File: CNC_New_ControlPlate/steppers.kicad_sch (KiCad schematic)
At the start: 6 parts

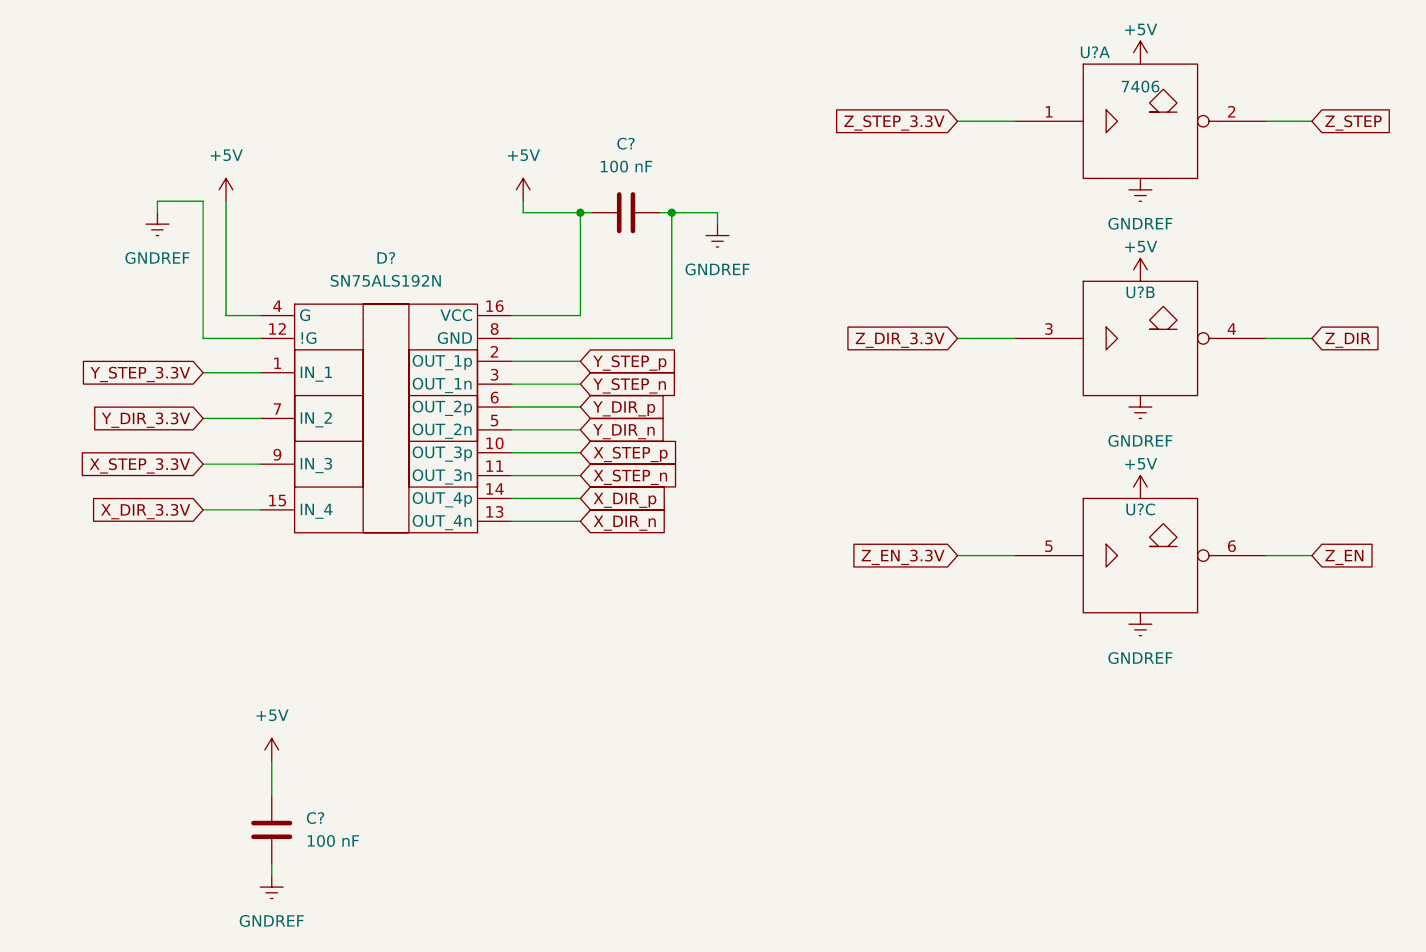
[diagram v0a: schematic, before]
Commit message: [*] Исправлены ошибки с выходами питания. [+] Добавлены обозначения элементов
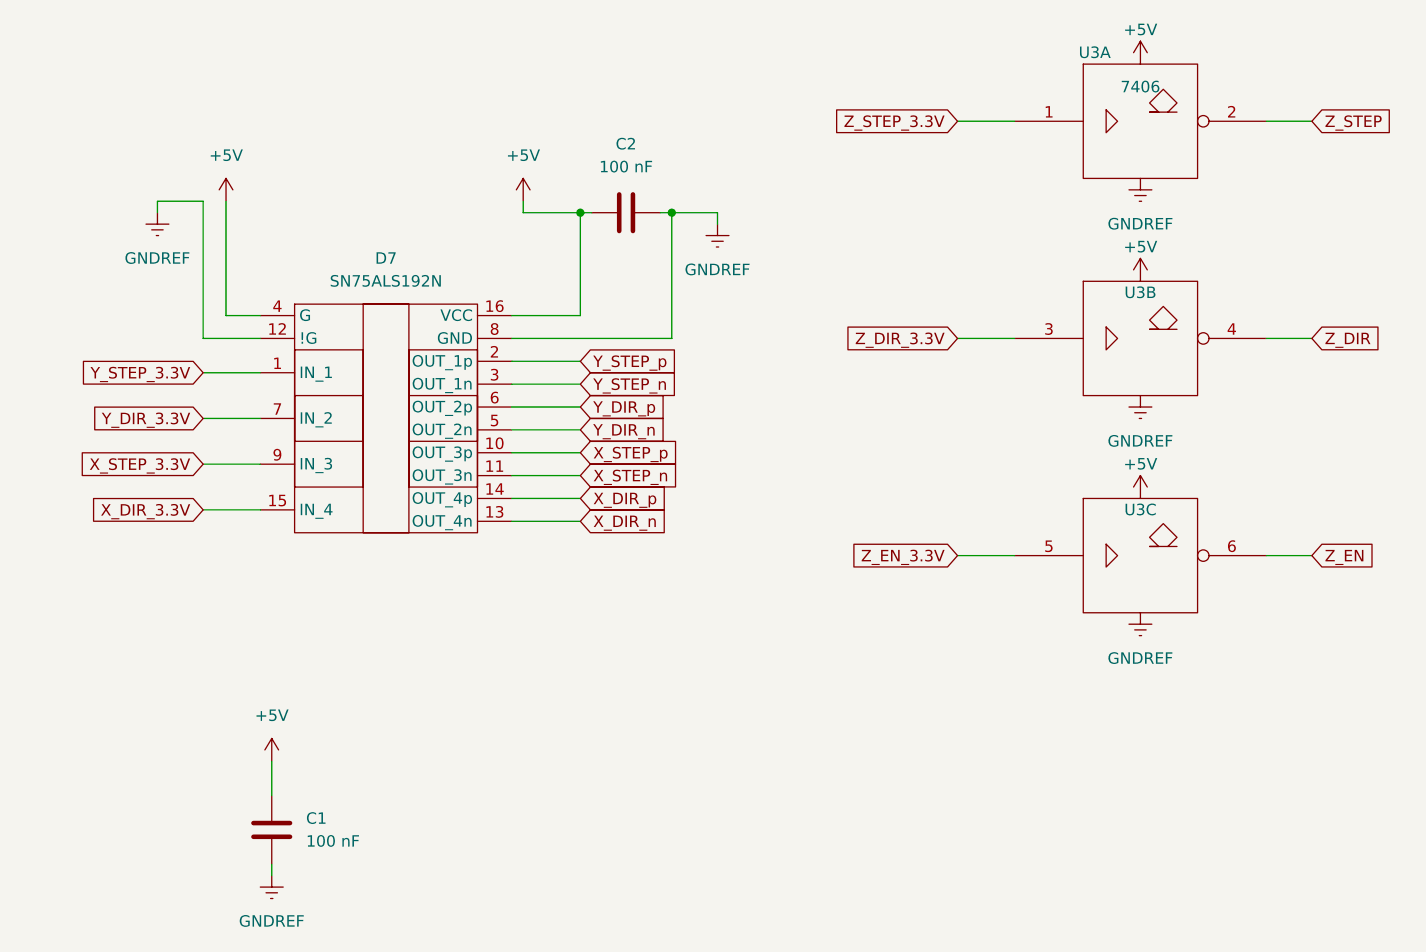
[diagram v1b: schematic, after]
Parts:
- gave numbers to parts that had none: 4
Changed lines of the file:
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@@
   (symbol (lib_id "power:+5V") (at 45.72 40.64 0) (unit 1)
     (in_bom yes) (on_board yes) (fields_autoplaced)
-    (property "Reference" "#PWR?" (id 0) (at 45.72 44.45 0)
+    (property "Reference" "#PWR027" (id 0) (at 45.72 44.45 0)
       (effects (font (size 1.27 1.27)) hide)
     )
@@
   (symbol (lib_id "power:+5V") (at 147.32 49.53 0) (unit 1)
     (in_bom yes) (on_board yes)
-    (property "Reference" "#PWR?" (id 0) (at 147.32 53.34 0)
+    (property "Reference" "#PWR034" (id 0) (at 147.32 53.34 0)
       (effects (font (size 1.27 1.27)) hide)
     )
@@
   (symbol (lib_id "74xx_IEEE:7406") (at 147.32 55.88 0) (unit 2)
     (in_bom yes) (on_board yes)
-    (property "Reference" "U?" (id 0) (at 147.32 50.8 0))
+    (property "Reference" "U3" (id 0) (at 147.32 50.8 0))
     (property "Value" "7406" (id 1) (at 147.32 46.99 0)
       (effects (font (size 1.27 1.27)) hide)
@@
   (symbol (lib_id "power:GNDREF") (at 147.32 62.23 0) (unit 1)
     (in_bom yes) (on_board yes) (fields_autoplaced)
-    (property "Reference" "#PWR?" (id 0) (at 147.32 68.58 0)
+    (property "Reference" "#PWR035" (id 0) (at 147.32 68.58 0)
       (effects (font (size 1.27 1.27)) hide)
     )
@@
   (symbol (lib_id "power:GNDREF") (at 38.1 41.91 0) (unit 1)
     (in_bom yes) (on_board yes) (fields_autoplaced)
-    (property "Reference" "#PWR?" (id 0) (at 38.1 48.26 0)
+    (property "Reference" "#PWR026" (id 0) (at 38.1 48.26 0)
       (effects (font (size 1.27 1.27)) hide)
     )
@@
   (symbol (lib_id "74xx_IEEE:7406") (at 147.32 31.75 0) (unit 1)
     (in_bom yes) (on_board yes)
-    (property "Reference" "U?" (id 0) (at 142.24 24.13 0))
+    (property "Reference" "U3" (id 0) (at 142.24 24.13 0))
     (property "Value" "7406" (id 1) (at 147.32 27.94 0))
     (property "Footprint" "" (id 2) (at 147.32 31.75 0)
@@
   (symbol (lib_id "power:GNDREF") (at 147.32 38.1 0) (unit 1)
     (in_bom yes) (on_board yes) (fields_autoplaced)
-    (property "Reference" "#PWR?" (id 0) (at 147.32 44.45 0)
+    (property "Reference" "#PWR033" (id 0) (at 147.32 44.45 0)
       (effects (font (size 1.27 1.27)) hide)
     )
@@
   (symbol (lib_id "power:+5V") (at 78.74 40.64 0) (unit 1)
     (in_bom yes) (on_board yes) (fields_autoplaced)
-    (property "Reference" "#PWR?" (id 0) (at 78.74 44.45 0)
+    (property "Reference" "#PWR030" (id 0) (at 78.74 44.45 0)
       (effects (font (size 1.27 1.27)) hide)
     )
@@
   (symbol (lib_id "EP2006:SN75ALS192N") (at 63.5 49.53 0) (unit 1)
     (in_bom yes) (on_board yes) (fields_autoplaced)
-    (property "Reference" "D?" (id 0) (at 63.5 46.99 0))
+    (property "Reference" "D7" (id 0) (at 63.5 46.99 0))
     (property "Value" "SN75ALS192N" (id 1) (at 63.5 49.53 0))
     (property "Footprint" "Package_DIP:DIP-16_W7.62mm_Socket" (id 2) (at 63.5 49.53 0)
@@
   (symbol (lib_id "Device:C") (at 90.17 41.91 90) (unit 1)
     (in_bom yes) (on_board yes) (fields_autoplaced)
-    (property "Reference" "C?" (id 0) (at 90.17 34.29 90))
+    (property "Reference" "C2" (id 0) (at 90.17 34.29 90))
     (property "Value" "100 nF" (id 1) (at 90.17 36.83 90))
     (property "Footprint" "Capacitor_SMD:C_0603_1608Metric_Pad1.08x0.95mm_HandSolder" (id 2) (at 93.98 40.9448 0)
@@
   (symbol (lib_id "Device:C") (at 50.8 110.49 180) (unit 1)
     (in_bom yes) (on_board yes) (fields_autoplaced)
-    (property "Reference" "C?" (id 0) (at 54.61 109.2199 0)
+    (property "Reference" "C1" (id 0) (at 54.61 109.2199 0)
       (effects (font (size 1.27 1.27)) (justify right))
     )
@@
   (symbol (lib_id "power:+5V") (at 147.32 73.66 0) (unit 1)
     (in_bom yes) (on_board yes)
-    (property "Reference" "#PWR?" (id 0) (at 147.32 77.47 0)
+    (property "Reference" "#PWR036" (id 0) (at 147.32 77.47 0)
       (effects (font (size 1.27 1.27)) hide)
     )
@@
   (symbol (lib_id "power:GNDREF") (at 100.33 43.18 0) (unit 1)
     (in_bom yes) (on_board yes) (fields_autoplaced)
-    (property "Reference" "#PWR?" (id 0) (at 100.33 49.53 0)
+    (property "Reference" "#PWR031" (id 0) (at 100.33 49.53 0)
       (effects (font (size 1.27 1.27)) hide)
     )
@@
   (symbol (lib_id "power:+5V") (at 147.32 25.4 0) (unit 1)
     (in_bom yes) (on_board yes)
-    (property "Reference" "#PWR?" (id 0) (at 147.32 29.21 0)
+    (property "Reference" "#PWR032" (id 0) (at 147.32 29.21 0)
       (effects (font (size 1.27 1.27)) hide)
     )
@@
   (symbol (lib_id "power:GNDREF") (at 147.32 86.36 0) (unit 1)
     (in_bom yes) (on_board yes) (fields_autoplaced)
-    (property "Reference" "#PWR?" (id 0) (at 147.32 92.71 0)
+    (property "Reference" "#PWR037" (id 0) (at 147.32 92.71 0)
       (effects (font (size 1.27 1.27)) hide)
     )
@@
   (symbol (lib_id "power:GNDREF") (at 50.8 115.57 0) (unit 1)
     (in_bom yes) (on_board yes) (fields_autoplaced)
-    (property "Reference" "#PWR?" (id 0) (at 50.8 121.92 0)
+    (property "Reference" "#PWR029" (id 0) (at 50.8 121.92 0)
       (effects (font (size 1.27 1.27)) hide)
     )
@@
   (symbol (lib_id "74xx_IEEE:7406") (at 147.32 80.01 0) (unit 3)
     (in_bom yes) (on_board yes)
-    (property "Reference" "U?" (id 0) (at 147.32 74.93 0))
+    (property "Reference" "U3" (id 0) (at 147.32 74.93 0))
     (property "Value" "7406" (id 1) (at 147.32 71.12 0)
       (effects (font (size 1.27 1.27)) hide)
@@
   (symbol (lib_id "power:+5V") (at 50.8 102.87 0) (unit 1)
     (in_bom yes) (on_board yes)
-    (property "Reference" "#PWR?" (id 0) (at 50.8 106.68 0)
-      (effects (font (size 1.27 1.27)) hide)
-    )
+    (property "Reference" "#PWR028" (id 0) (at 50.8 106.68 0)
+      (effects (font (size 1.27 1.27)) hide)
+    )

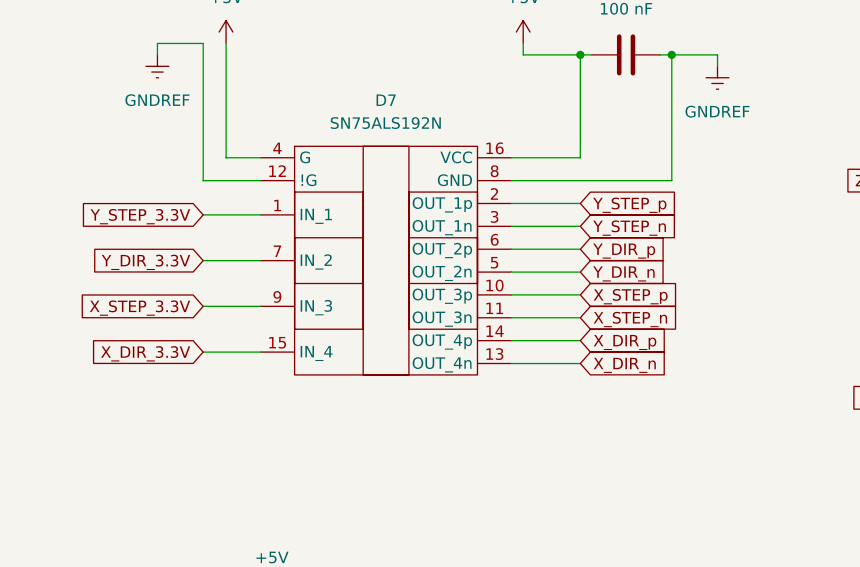
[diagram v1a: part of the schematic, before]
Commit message: [*] Порядок выводов на разъёме Others [*] Порядок выводов на разъёме Pause [*] Порядок подключения каналов на драйвере диф. линий [+] Начата расстановка pcb схемы
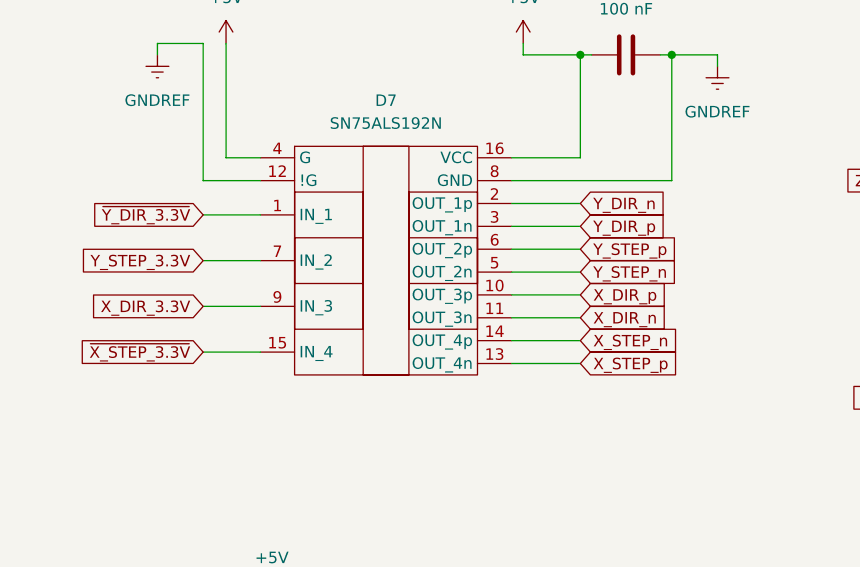
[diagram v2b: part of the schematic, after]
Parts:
- U3: footprint (none) -> Package_DIP:DIP-14_W7.62mm_Socket
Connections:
- net X_STEP_3.3V is gone; now on net X_DIR_3.3V: D7.9 (IN_3)
- net Y_DIR_3.3V is gone; now on net Y_STEP_3.3V: D7.7 (IN_2)
- net X_DIR_3.3V: no longer D7.15 (IN_4)
- net X_DIR_n: now also D7.11 (OUT_3n); no longer D7.13 (OUT_4n)
- net X_DIR_p: now also D7.10 (OUT_3p); no longer D7.14 (OUT_4p)
- net X_STEP_n: now also D7.14 (OUT_4p); no longer D7.11 (OUT_3n)
- net X_STEP_p: now also D7.13 (OUT_4n); no longer D7.10 (OUT_3p)
- net Y_DIR_n: now also D7.2 (OUT_1p); no longer D7.5 (OUT_2n)
- net Y_DIR_p: now also D7.3 (OUT_1n); no longer D7.6 (OUT_2p)
- net Y_STEP_3.3V: no longer D7.1 (IN_1)
- net Y_STEP_n: now also D7.5 (OUT_2n); no longer D7.3 (OUT_1n)
- net Y_STEP_p: now also D7.6 (OUT_2p); no longer D7.2 (OUT_1p)
- new net ~{X_STEP_3.3V}: D7.15 (IN_4)
- new net ~{Y_DIR_3.3V}: D7.1 (IN_1)
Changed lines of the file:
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@@
     )
   )
-  (global_label "X_DIR_n" (shape input) (at 85.09 76.2 0) (fields_autoplaced)
-    (effects (font (size 1.27 1.27)) (justify left))
-    (property "Intersheet References" "${INTERSHEET_REFS}" (id 0) (at 94.9417 76.1206 0)
+  (global_label "X_DIR_n" (shape input) (at 85.09 71.12 0) (fields_autoplaced)
+    (effects (font (size 1.27 1.27)) (justify left))
+    (property "Intersheet References" "${INTERSHEET_REFS}" (id 0) (at 94.9417 71.0406 0)
       (effects (font (size 1.27 1.27)) (justify left) hide)
     )
@@
     )
   )
-  (global_label "X_DIR_p" (shape input) (at 85.09 73.66 0) (fields_autoplaced)
-    (effects (font (size 1.27 1.27)) (justify left))
-    (property "Intersheet References" "${INTERSHEET_REFS}" (id 0) (at 94.9417 73.5806 0)
-      (effects (font (size 1.27 1.27)) (justify left) hide)
-    )
-  )
-  (global_label "Y_STEP_3.3V" (shape input) (at 43.18 59.69 180) (fields_autoplaced)
-    (effects (font (size 1.27 1.27)) (justify right))
-    (property "Intersheet References" "${INTERSHEET_REFS}" (id 0) (at 29.0345 59.6106 0)
-      (effects (font (size 1.27 1.27)) (justify right) hide)
-    )
-  )
-  (global_label "Y_DIR_3.3V" (shape input) (at 43.18 64.77 180) (fields_autoplaced)
-    (effects (font (size 1.27 1.27)) (justify right))
-    (property "Intersheet References" "${INTERSHEET_REFS}" (id 0) (at 30.4859 64.6906 0)
-      (effects (font (size 1.27 1.27)) (justify right) hide)
-    )
-  )
-  (global_label "X_STEP_3.3V" (shape input) (at 43.18 69.85 180) (fields_autoplaced)
-    (effects (font (size 1.27 1.27)) (justify right))
-    (property "Intersheet References" "${INTERSHEET_REFS}" (id 0) (at 28.9136 69.7706 0)
-      (effects (font (size 1.27 1.27)) (justify right) hide)
-    )
-  )
-  (global_label "Y_DIR_p" (shape input) (at 85.09 63.5 0) (fields_autoplaced)
-    (effects (font (size 1.27 1.27)) (justify left))
-    (property "Intersheet References" "${INTERSHEET_REFS}" (id 0) (at 94.8207 63.4206 0)
-      (effects (font (size 1.27 1.27)) (justify left) hide)
-    )
-  )
-  (global_label "X_STEP_n" (shape input) (at 85.09 71.12 0) (fields_autoplaced)
-    (effects (font (size 1.27 1.27)) (justify left))
-    (property "Intersheet References" "${INTERSHEET_REFS}" (id 0) (at 96.3931 71.0406 0)
-      (effects (font (size 1.27 1.27)) (justify left) hide)
-    )
-  )
-  (global_label "X_DIR_3.3V" (shape input) (at 43.18 74.93 180) (fields_autoplaced)
-    (effects (font (size 1.27 1.27)) (justify right))
-    (property "Intersheet References" "${INTERSHEET_REFS}" (id 0) (at 30.365 74.8506 0)
-      (effects (font (size 1.27 1.27)) (justify right) hide)
-    )
-  )
-  (global_label "Y_STEP_p" (shape input) (at 85.09 58.42 0) (fields_autoplaced)
-    (effects (font (size 1.27 1.27)) (justify left))
-    (property "Intersheet References" "${INTERSHEET_REFS}" (id 0) (at 96.2721 58.3406 0)
-      (effects (font (size 1.27 1.27)) (justify left) hide)
-    )
-  )
-  (global_label "Y_DIR_n" (shape input) (at 85.09 66.04 0) (fields_autoplaced)
-    (effects (font (size 1.27 1.27)) (justify left))
-    (property "Intersheet References" "${INTERSHEET_REFS}" (id 0) (at 94.8207 65.9606 0)
-      (effects (font (size 1.27 1.27)) (justify left) hide)
-    )
-  )
-  (global_label "Y_STEP_n" (shape input) (at 85.09 60.96 0) (fields_autoplaced)
-    (effects (font (size 1.27 1.27)) (justify left))
-    (property "Intersheet References" "${INTERSHEET_REFS}" (id 0) (at 96.2721 60.8806 0)
-      (effects (font (size 1.27 1.27)) (justify left) hide)
-    )
-  )
-  (global_label "X_STEP_p" (shape input) (at 85.09 68.58 0) (fields_autoplaced)
-    (effects (font (size 1.27 1.27)) (justify left))
-    (property "Intersheet References" "${INTERSHEET_REFS}" (id 0) (at 96.3931 68.5006 0)
+  (global_label "X_DIR_p" (shape input) (at 85.09 68.58 0) (fields_autoplaced)
+    (effects (font (size 1.27 1.27)) (justify left))
+    (property "Intersheet References" "${INTERSHEET_REFS}" (id 0) (at 94.9417 68.5006 0)
+      (effects (font (size 1.27 1.27)) (justify left) hide)
+    )
+  )
+  (global_label "Y_STEP_3.3V" (shape input) (at 43.18 64.77 180) (fields_autoplaced)
+    (effects (font (size 1.27 1.27)) (justify right))
+    (property "Intersheet References" "${INTERSHEET_REFS}" (id 0) (at 29.0345 64.6906 0)
+      (effects (font (size 1.27 1.27)) (justify right) hide)
+    )
+  )
+  (global_label "~{Y_DIR_3.3V}" (shape input) (at 43.18 59.69 180) (fields_autoplaced)
+    (effects (font (size 1.27 1.27)) (justify right))
+    (property "Intersheet References" "${INTERSHEET_REFS}" (id 0) (at 30.4859 59.6106 0)
+      (effects (font (size 1.27 1.27)) (justify right) hide)
+    )
+  )
+  (global_label "~{X_STEP_3.3V}" (shape input) (at 43.18 74.93 180) (fields_autoplaced)
+    (effects (font (size 1.27 1.27)) (justify right))
+    (property "Intersheet References" "${INTERSHEET_REFS}" (id 0) (at 28.9136 74.8506 0)
+      (effects (font (size 1.27 1.27)) (justify right) hide)
+    )
+  )
+  (global_label "Y_DIR_p" (shape input) (at 85.09 60.96 0) (fields_autoplaced)
+    (effects (font (size 1.27 1.27)) (justify left))
+    (property "Intersheet References" "${INTERSHEET_REFS}" (id 0) (at 94.8207 60.8806 0)
+      (effects (font (size 1.27 1.27)) (justify left) hide)
+    )
+  )
+  (global_label "X_STEP_n" (shape input) (at 85.09 73.66 0) (fields_autoplaced)
+    (effects (font (size 1.27 1.27)) (justify left))
+    (property "Intersheet References" "${INTERSHEET_REFS}" (id 0) (at 96.3931 73.5806 0)
+      (effects (font (size 1.27 1.27)) (justify left) hide)
+    )
+  )
+  (global_label "X_DIR_3.3V" (shape input) (at 43.18 69.85 180) (fields_autoplaced)
+    (effects (font (size 1.27 1.27)) (justify right))
+    (property "Intersheet References" "${INTERSHEET_REFS}" (id 0) (at 30.365 69.7706 0)
+      (effects (font (size 1.27 1.27)) (justify right) hide)
+    )
+  )
+  (global_label "Y_STEP_p" (shape input) (at 85.09 63.5 0) (fields_autoplaced)
+    (effects (font (size 1.27 1.27)) (justify left))
+    (property "Intersheet References" "${INTERSHEET_REFS}" (id 0) (at 96.2721 63.4206 0)
+      (effects (font (size 1.27 1.27)) (justify left) hide)
+    )
+  )
+  (global_label "Y_DIR_n" (shape input) (at 85.09 58.42 0) (fields_autoplaced)
+    (effects (font (size 1.27 1.27)) (justify left))
+    (property "Intersheet References" "${INTERSHEET_REFS}" (id 0) (at 94.8207 58.3406 0)
+      (effects (font (size 1.27 1.27)) (justify left) hide)
+    )
+  )
+  (global_label "Y_STEP_n" (shape input) (at 85.09 66.04 0) (fields_autoplaced)
+    (effects (font (size 1.27 1.27)) (justify left))
+    (property "Intersheet References" "${INTERSHEET_REFS}" (id 0) (at 96.2721 65.9606 0)
+      (effects (font (size 1.27 1.27)) (justify left) hide)
+    )
+  )
+  (global_label "X_STEP_p" (shape input) (at 85.09 76.2 0) (fields_autoplaced)
+    (effects (font (size 1.27 1.27)) (justify left))
+    (property "Intersheet References" "${INTERSHEET_REFS}" (id 0) (at 96.3931 76.1206 0)
       (effects (font (size 1.27 1.27)) (justify left) hide)
     )
@@
       (effects (font (size 1.27 1.27)) hide)
     )
-    (property "Footprint" "" (id 2) (at 147.32 55.88 0)
+    (property "Footprint" "Package_DIP:DIP-14_W7.62mm_Socket" (id 2) (at 147.32 55.88 0)
       (effects (font (size 1.27 1.27)) hide)
     )
@@
     (property "Reference" "U3" (id 0) (at 142.24 24.13 0))
     (property "Value" "7406" (id 1) (at 147.32 27.94 0))
-    (property "Footprint" "" (id 2) (at 147.32 31.75 0)
+    (property "Footprint" "Package_DIP:DIP-14_W7.62mm_Socket" (id 2) (at 147.32 31.75 0)
       (effects (font (size 1.27 1.27)) hide)
     )
@@
       (effects (font (size 1.27 1.27)) hide)
     )
-    (property "Footprint" "" (id 2) (at 147.32 80.01 0)
-      (effects (font (size 1.27 1.27)) hide)
-    )
+    (property "Footprint" "Package_DIP:DIP-14_W7.62mm_Socket" (id 2) (at 147.32 80.01 0)
+      (effects (font (size 1.27 1.27)) hide)
+    )
